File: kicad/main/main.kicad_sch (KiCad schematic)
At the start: 8 parts, among them SW1 SW_SPDT_312, U1 HC-SR04, U2 DFR0654

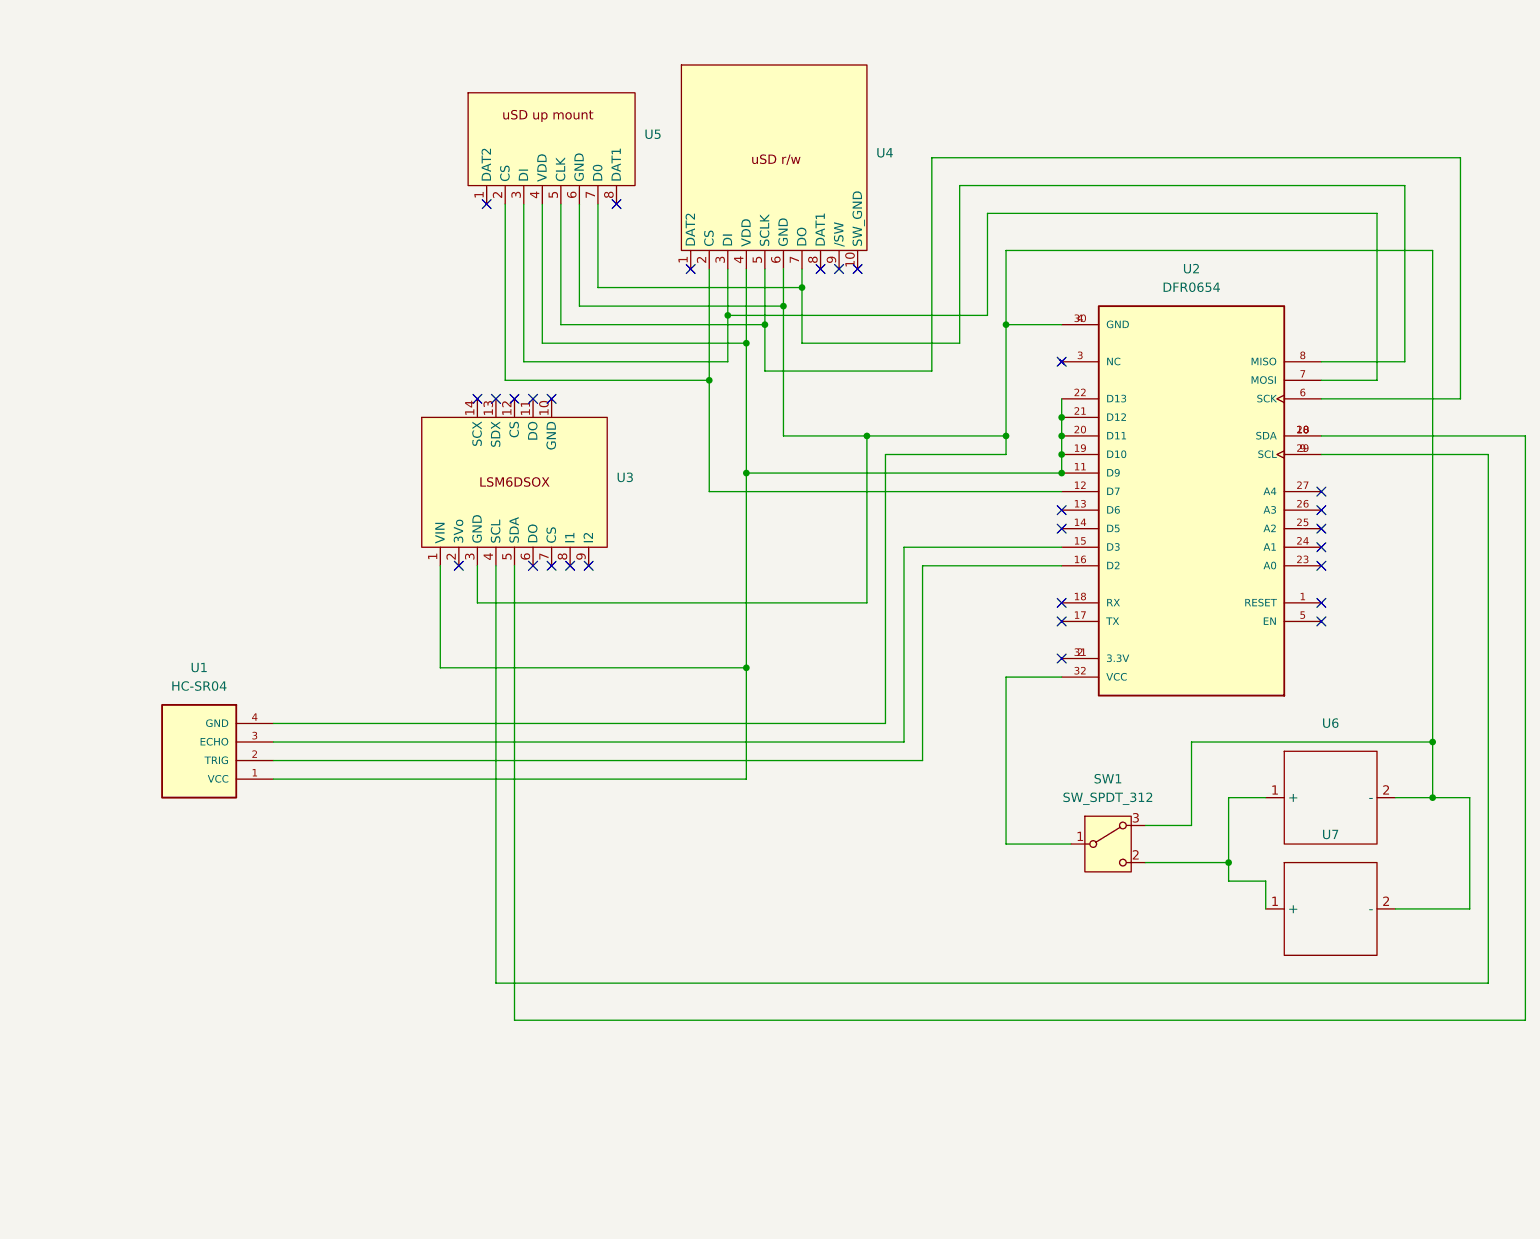
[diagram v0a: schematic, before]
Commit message: cleaned up PCB design
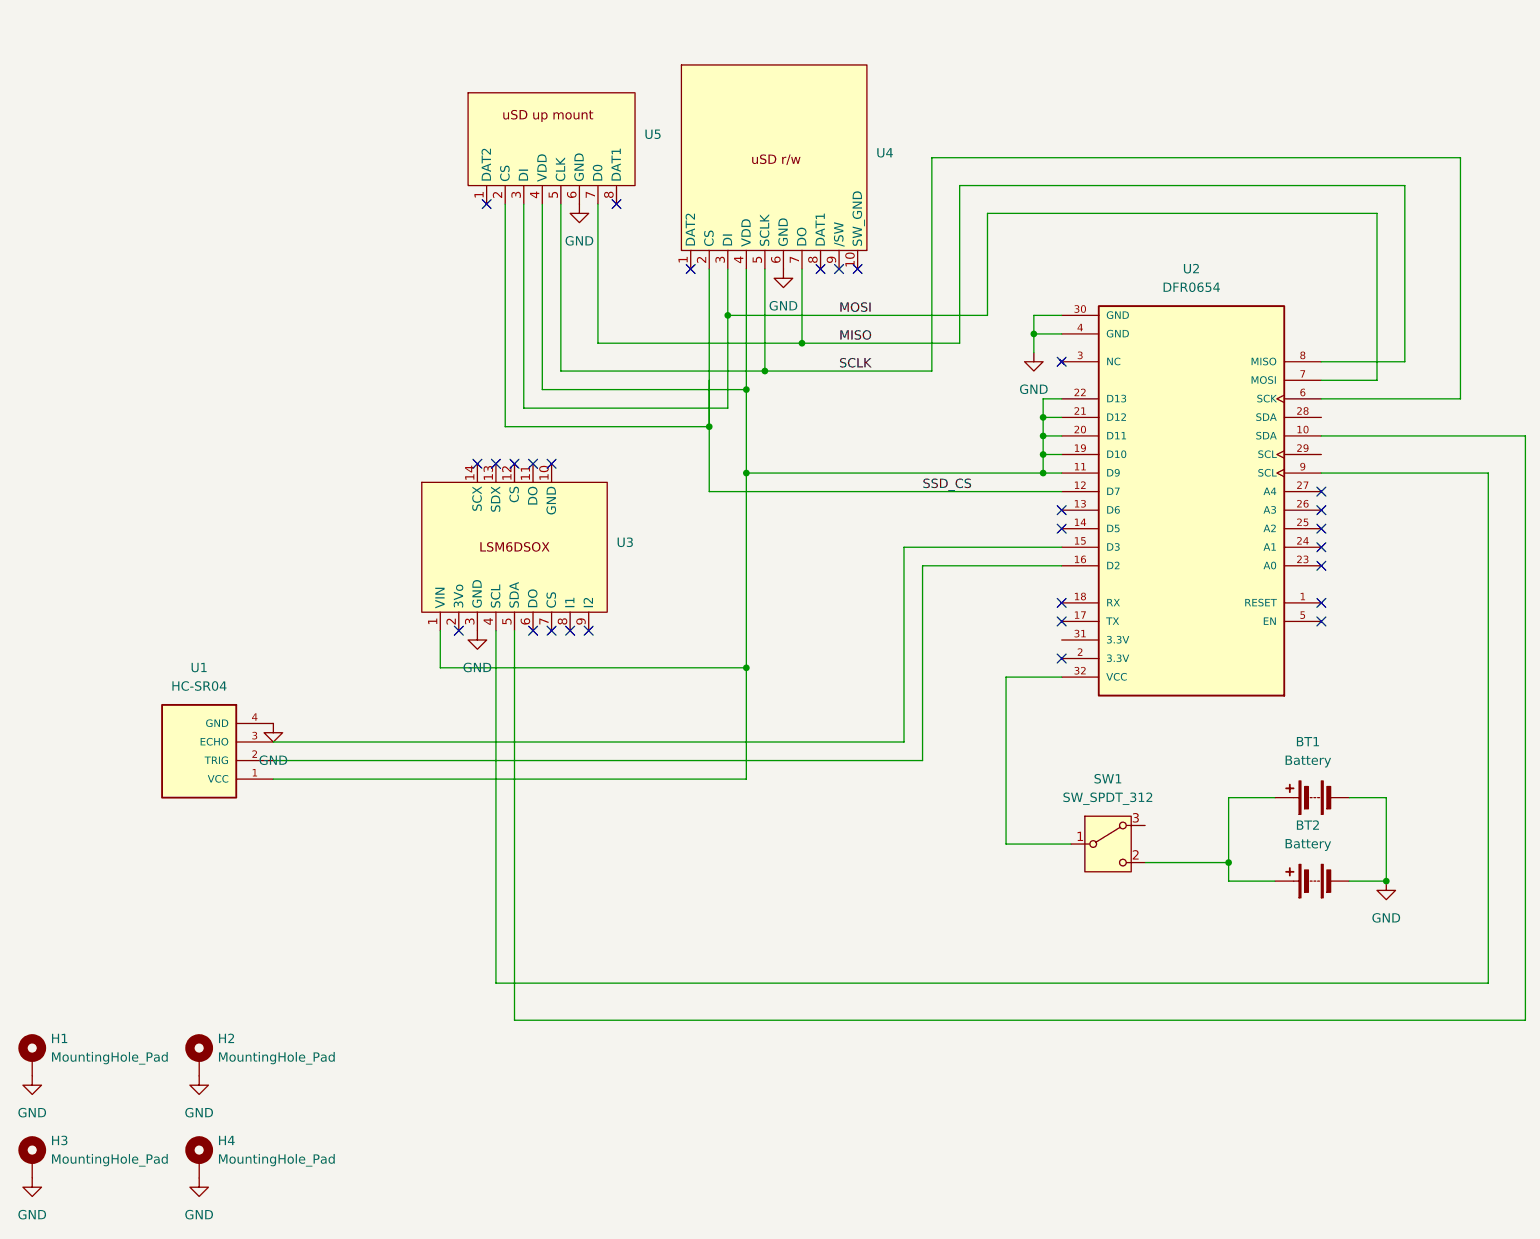
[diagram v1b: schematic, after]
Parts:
- removed U6, U7: ~, singing foot:battery_holes, symbol Singing Poles Symbols:Battery
- added BT1, BT2: Battery, Connector_PinHeader_2.54mm:PinHeader_1x02_P2.54mm_Vertical, symbol Device:Battery
- added H1, H2, H4: MountingHole_Pad, MountingHole:MountingHole_3.2mm_M3_DIN965_Pad, symbol Mechanical:MountingHole_Pad
- added H3: MountingHole_Pad, symbol Mechanical:MountingHole_Pad
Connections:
- net at SW1.2 (C): now also BT1.1 (+), BT2.1 (+)
- net GND: now reaches U1.4 (GND), U2.30 (GND), U2.4 (GND), U3.3 (GND), U4.6 (GND), U5.6 (GND)
- net GND: now also BT1.2 (-), BT2.2 (-), H1.1, H2.1, H3.1, H4.1; no longer SW1.3 (A)
- net SSD_CS: now reaches U2.12 (D7), U4.2 (CS), U5.2 (CS)
- net MOSI: now reaches U2.7 (MOSI), U4.3 (DI), U5.3 (DI)
- net SCLK: now reaches U2.6 (SCK), U4.5 (SCLK), U5.5 (CLK)
- net MISO: now reaches U2.8 (MISO), U4.7 (DO), U5.7 (D0)
- net at U2.10 (SDA), U3.5 (SDA): no longer U2.28 (SDA)
- net at U2.2 (3.3V): no longer U2.31 (3.3V)
- net at U2.9 (SCL), U3.4 (SCL): no longer U2.29 (SCL)
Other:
- moved on the sheet: U3

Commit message: added mounting holes?
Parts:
- H3: footprint (none) -> MountingHole:MountingHole_3.2mm_M3_DIN965_Pad
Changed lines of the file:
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@@
 			)
 		)
-		(property "Footprint" ""
+		(property "Footprint" "MountingHole:MountingHole_3.2mm_M3_DIN965_Pad"
 			(at 26.67 177.8 0)
 			(effects

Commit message: as sent to PCBWay
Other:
- note added: "(use only one)"
- note added: "3 x AA"
- note added: "Accelerometer Module"
- note added: "ESP32 MCU Module"
- note added: "Micro-SD Socket"
- note added: "Micro-SD socket module"
- note added: "Ultrasonic Rangefinder"
- company: (none) -> McGill University Physics Department
- title: (none) -> Brachi PCB
- moved on the sheet: BT2
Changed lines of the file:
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@@
 	(generator "eeschema")
 	(generator_version "8.0")
-	(paper "A4")
+	(paper "A")
+	(title_block
+		(title "Brachi PCB")
+		(date "2024-08-14")
+		(rev "1.0")
+		(company "McGill University Physics Department")
+		(comment 1 "McGill Radio Lab")
+		(comment 2 "Felix St-Amour & Eamon Egan")
+	)
 	(junction
 		(at 165.1 83.82)
@@
 	)
 	(junction
-		(at 212.09 139.7)
+		(at 212.09 144.78)
 		(diameter 0)
 		(color 0 0 0 0)
@@
 	(wire
 		(pts
-			(xy 207.01 128.27) (xy 212.09 128.27)
+			(xy 212.09 128.27) (xy 212.09 144.78)
 		)
 		(stroke
@@
 	(wire
 		(pts
-			(xy 190.5 139.7) (xy 196.85 139.7)
+			(xy 190.5 144.78) (xy 196.85 144.78)
 		)
 		(stroke
@@
 	(wire
 		(pts
+			(xy 212.09 128.27) (xy 207.01 128.27)
+		)
+		(stroke
+			(width 0)
+			(type default)
+		)
+	)
+	(wire
+		(pts
 			(xy 190.5 128.27) (xy 196.85 128.27)
 		)
@@
 	(wire
 		(pts
-			(xy 212.09 128.27) (xy 212.09 139.7)
-		)
-		(stroke
-			(width 0)
-			(type default)
-		)
-	)
-	(wire
-		(pts
-			(xy 190.5 139.7) (xy 190.5 137.16)
+			(xy 190.5 144.78) (xy 190.5 137.16)
 		)
 		(stroke
@@
 	(wire
 		(pts
-			(xy 212.09 139.7) (xy 207.01 139.7)
+			(xy 212.09 144.78) (xy 207.01 144.78)
 		)
 		(stroke
@@
 			(type default)
 			(color 255 0 0 1)
+		)
+	)
+	(text "Micro-SD socket module"
+		(exclude_from_sim no)
+		(at 128.016 25.908 0)
+		(effects
+			(font
+				(size 1.27 1.27)
+			)
+		)
+	)
+	(text "ESP32 MCU Module"
+		(exclude_from_sim no)
+		(at 184.658 54.102 0)
+		(effects
+			(font
+				(size 1.27 1.27)
+			)
+		)
+	)
+	(text "3 x AA"
+		(exclude_from_sim no)
+		(at 208.534 140.208 0)
+		(effects
+			(font
+				(size 1.27 1.27)
+			)
+		)
+	)
+	(text "(use only one)"
+		(exclude_from_sim no)
+		(at 109.474 22.606 0)
+		(effects
+			(font
+				(size 1.27 1.27)
+			)
+		)
+	)
+	(text "3 x AA"
+		(exclude_from_sim no)
+		(at 208.534 123.952 0)
+		(effects
+			(font
+				(size 1.27 1.27)
+			)
+		)
+	)
+	(text "Micro-SD Socket"
+		(exclude_from_sim no)
+		(at 94.234 29.21 0)
+		(effects
+			(font
+				(size 1.27 1.27)
+			)
+		)
+	)
+	(text "Ultrasonic Rangefinder"
+		(exclude_from_sim no)
+		(at 51.308 108.712 0)
+		(effects
+			(font
+				(size 1.27 1.27)
+			)
+		)
+	)
+	(text "Accelerometer Module"
+		(exclude_from_sim no)
+		(at 92.71 80.518 0)
+		(effects
+			(font
+				(size 1.27 1.27)
+			)
 		)
 	)
@@
 	(symbol
 		(lib_id "power:GND")
-		(at 212.09 139.7 0)
+		(at 212.09 144.78 0)
 		(unit 1)
 		(exclude_from_sim no)
@@
 		(fields_autoplaced yes)
 		(property "Reference" "#PWR05"
-			(at 212.09 146.05 0)
+			(at 212.09 151.13 0)
 			(effects
 				(font
@@
 		)
 		(property "Value" "GND"
+			(at 212.09 149.86 0)
+			(effects
+				(font
+					(size 1.27 1.27)
+				)
+			)
+		)
+		(property "Footprint" ""
 			(at 212.09 144.78 0)
 			(effects
@@
 					(size 1.27 1.27)
 				)
-			)
-		)
-		(property "Footprint" ""
-			(at 212.09 139.7 0)
-			(effects
-				(font
-					(size 1.27 1.27)
-				)
 				(hide yes)
 			)
 		)
 		(property "Datasheet" ""
-			(at 212.09 139.7 0)
+			(at 212.09 144.78 0)
 			(effects
 				(font
@@
 		)
 		(property "Description" "Power symbol creates a global label with name \"GND\" , ground"
-			(at 212.09 139.7 0)
+			(at 212.09 144.78 0)
 			(effects
 				(font
@@
 	(symbol
 		(lib_id "Device:Battery")
-		(at 201.93 139.7 90)
+		(at 201.93 144.78 90)
 		(unit 1)
 		(exclude_from_sim no)
@@
 		(fields_autoplaced yes)
 		(property "Reference" "BT2"
-			(at 201.3585 132.08 90)
+			(at 201.3585 137.16 90)
 			(effects
 				(font
@@
 		)
 		(property "Value" "Battery"
-			(at 201.3585 134.62 90)
+			(at 201.3585 139.7 90)
 			(effects
 				(font
@@
 		)
 		(property "Footprint" "Connector_PinHeader_2.54mm:PinHeader_1x02_P2.54mm_Vertical"
-			(at 200.406 139.7 90)
+			(at 200.406 144.78 90)
 			(effects
 				(font
@@
 		)
 		(property "Datasheet" "~"
-			(at 200.406 139.7 90)
+			(at 200.406 144.78 90)
 			(effects
 				(font
@@
 		)
 		(property "Description" "Multiple-cell battery"
-			(at 201.93 139.7 0)
-			(effects
-				(font
+			(at 201.93 144.78 0)
+			(effects
+				(font
